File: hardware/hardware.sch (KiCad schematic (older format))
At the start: 23 parts, among them J1 6P6C, J2 RJ45_LED_Shielded, Q1 BUK7M33-60EX, U1 Teensy4.1_DEV-16771, U2 LT1910, U3 OKI, U4 OKI-78SR-3.3_1.5-W36H-C

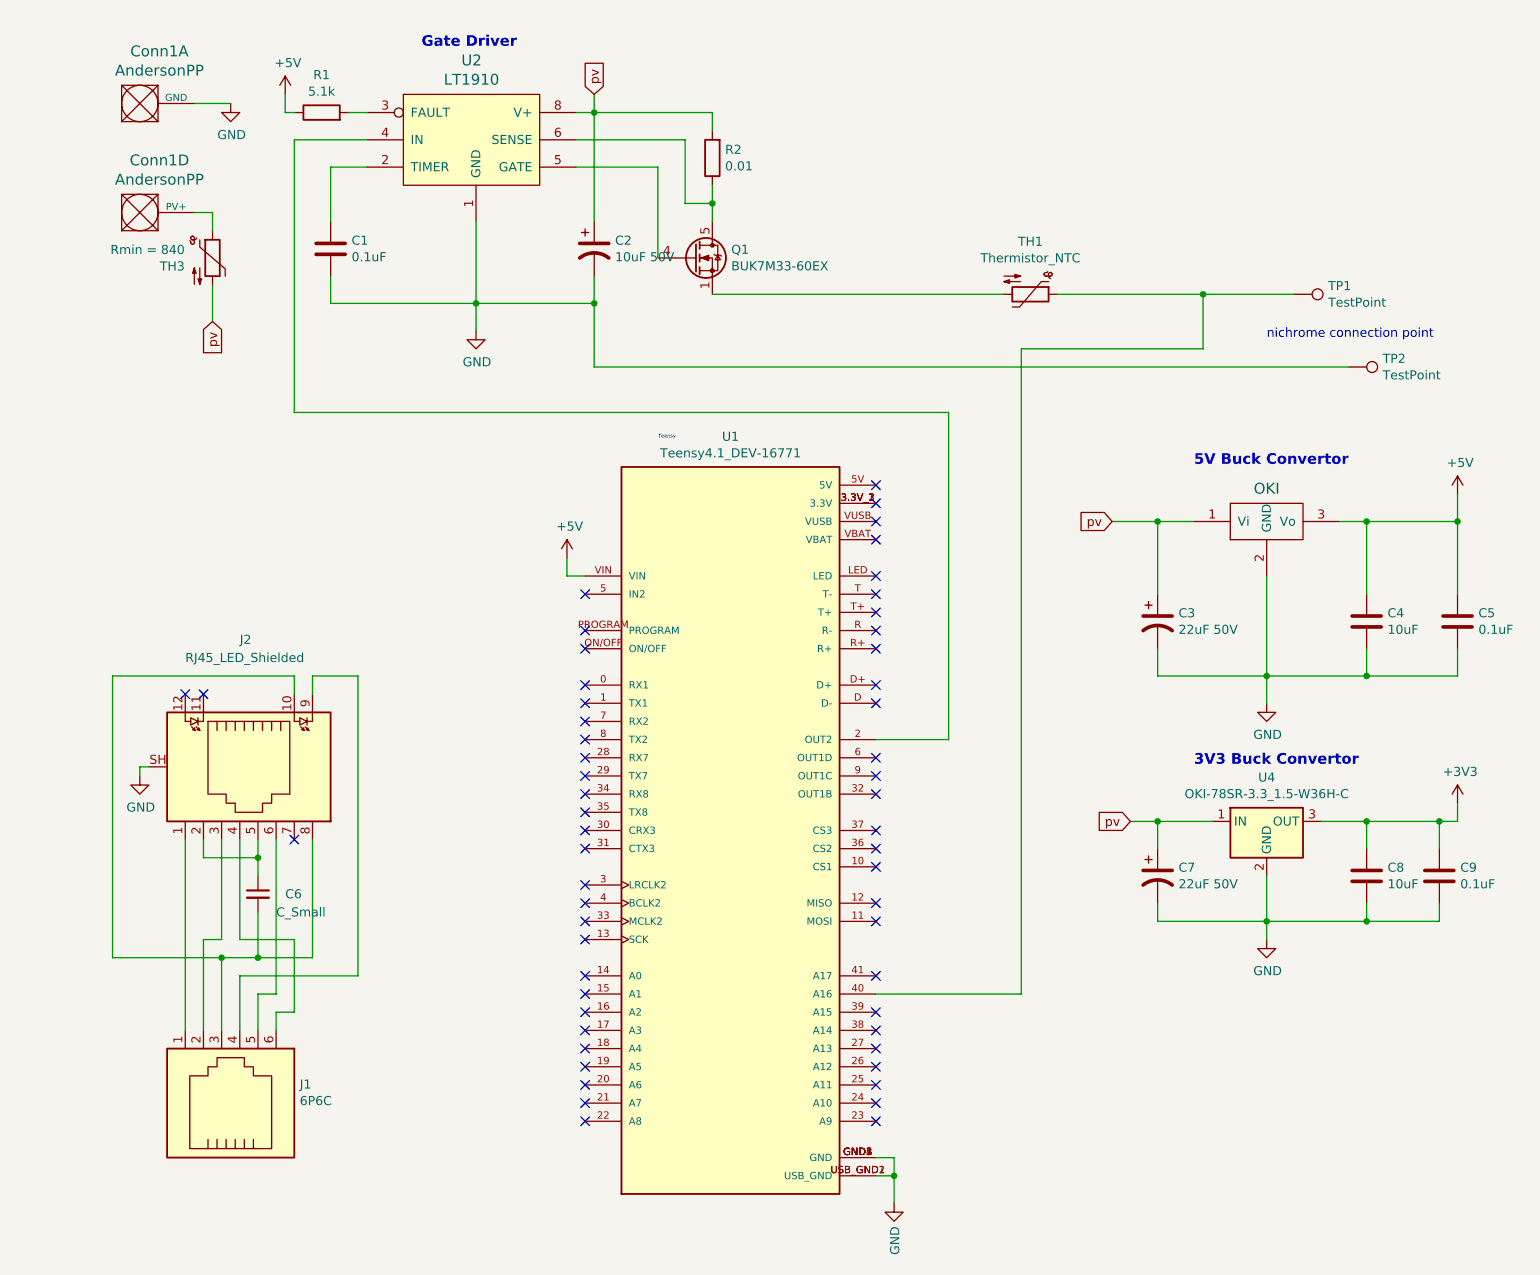
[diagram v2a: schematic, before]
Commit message: Fixed ethernet circuit and general cleaning
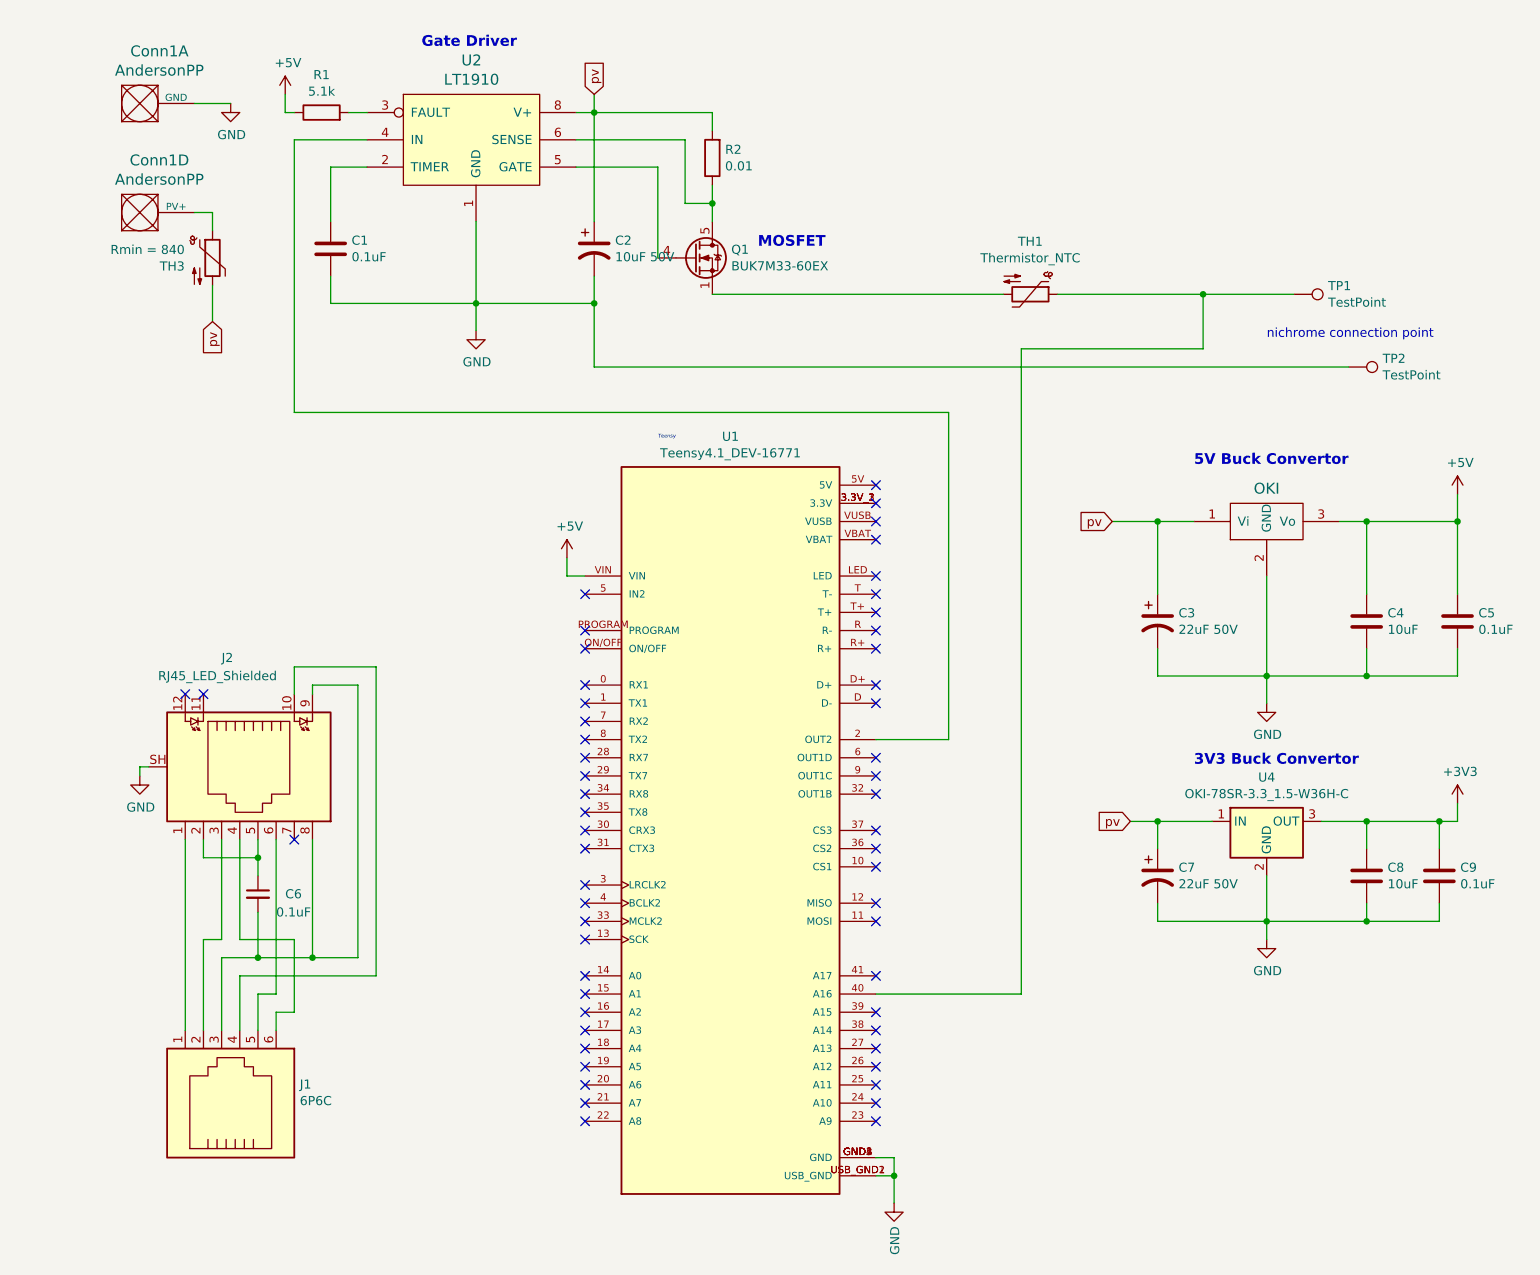
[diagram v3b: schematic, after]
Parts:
- C6: value C_Small -> 0.1uF
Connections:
- net at C6.2, J1.3, J2.8: now also J2.9; no longer J2.10
- net at J1.4: now also J2.10; no longer J2.9
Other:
- note added: "MOSFET"
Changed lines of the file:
@@
 U 1 1 61651929
 P 1350 4550
-F 0 "J2" V 650 4550 50  0000 L CNN
-F 1 "RJ45_LED_Shielded" V 750 4250 50  0000 L CNN
+F 0 "J2" V 750 4450 50  0000 L CNN
+F 1 "RJ45_LED_Shielded" V 850 4100 50  0000 L CNN
 F 2 "" V 1350 4575 50  0001 C CNN
 F 3 "~" V 1350 4575 50  0001 C CNN
@@
 $EndComp
 Wire Wire Line
-	2000 4050 1750 4050
+	2000 4100 1750 4100
 NoConn ~ 1650 4950
 NoConn ~ 1050 4150
@@
 P 1450 5250
 F 0 "C6" H 1600 5250 50  0000 L CNN
-F 1 "C_Small" H 1550 5150 50  0000 L CNN
+F 1 "0.1uF" H 1550 5150 50  0000 L CNN
 F 2 "" H 1450 5250 50  0001 C CNN
 F 3 "~" H 1450 5250 50  0001 C CNN
@@
 Wire Wire Line
 	1250 5500 1150 5500
-Wire Wire Line
-	1350 5700 2000 5700
 Wire Wire Line
 	1450 5800 1550 5800
@@
 	1350 5500 1350 4950
 Wire Wire Line
-	1250 5600 650  5600
+	1750 4100 1750 4150
 Wire Wire Line
-	650  5600 650  4050
+	1750 5600 2000 5600
 Wire Wire Line
-	650  4050 1650 4050
+	2000 5600 2000 4100
+Connection ~ 1750 5600
 Wire Wire Line
-	1650 4050 1650 4150
-Connection ~ 1250 5600
+	2100 5700 2100 4000
 Wire Wire Line
-	2000 4050 2000 5700
+	2100 4000 1650 4000
 Wire Wire Line
-	1750 4050 1750 4150
+	1350 5700 2100 5700
+Wire Wire Line
+	1650 4000 1650 4150
+Text Notes 4200 1700 0    59   ~ 12
+MOSFET
 $EndSCHEMATC

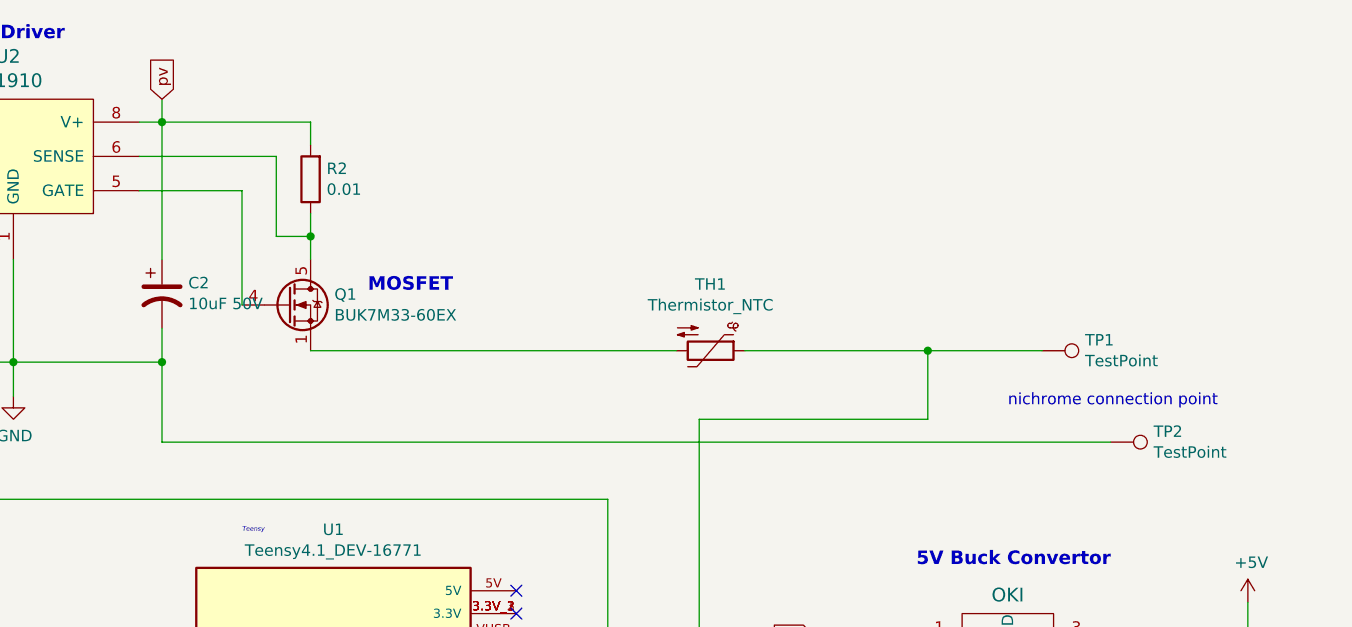
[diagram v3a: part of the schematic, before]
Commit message: Nichrome Cleanup
Cleaned up circuit for PDR and assigned R for wire
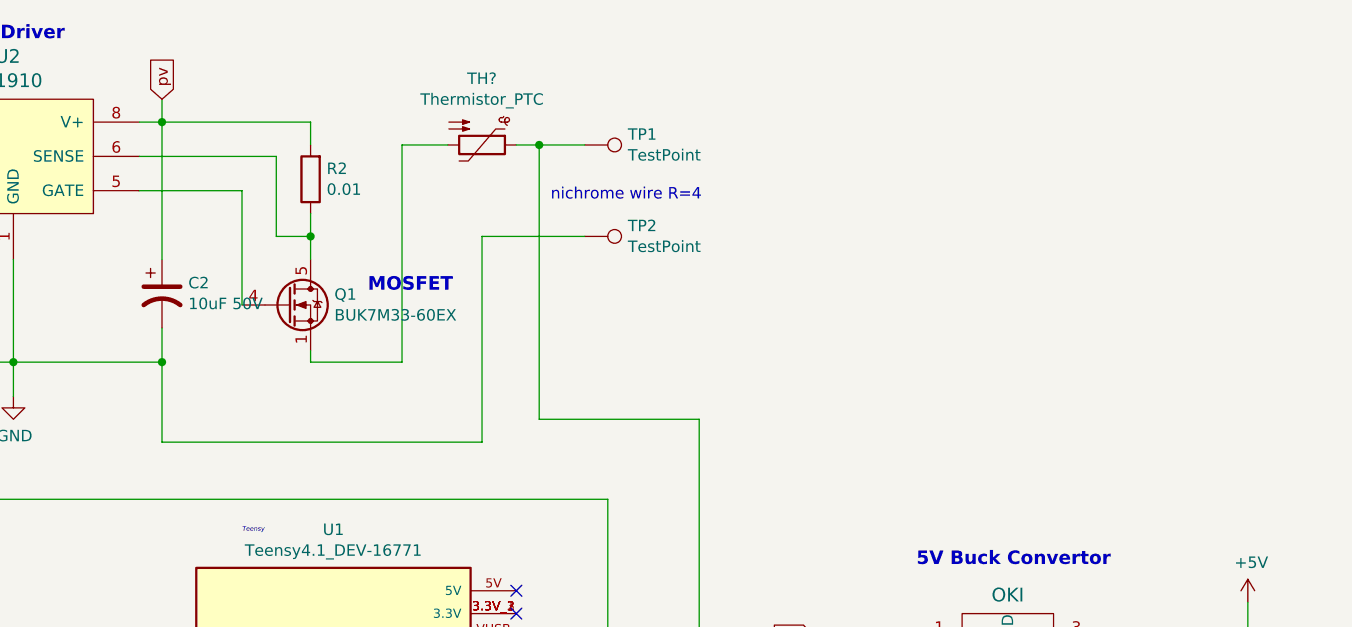
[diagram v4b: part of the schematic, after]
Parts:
- removed TH1: Thermistor_NTC, symbol Device:Thermistor_NTC
- added TH?: Thermistor_PTC, symbol Device:Thermistor_PTC
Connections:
- net at TP1.1, U1.40 (A16): now also TH?.1
- net at Q1.1 (S), Q1.2 (S), Q1.3 (S): now also TH?.2
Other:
- note added: "nichrome wire R=4"
- note removed: "nichrome connection point"
- moved on the sheet: TP1, TP2
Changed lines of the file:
@@
 Wire Wire Line
 	3150 3500 3250 3500
-$Comp
-L Device:Thermistor_NTC TH1
-U 1 1 615942DB
-P 5700 1950
-F 0 "TH1" V 5410 1950 50  0000 C CNN
-F 1 "Thermistor_NTC" V 5501 1950 50  0000 C CNN
-F 2 "" H 5700 2000 50  0001 C CNN
-F 3 "~" H 5700 2000 50  0001 C CNN
-	1    5700 1950
-	0    1    1    0
-$EndComp
 Wire Wire Line
 	5250 2600 1650 2600
@@
 Wire Wire Line
 	5650 5800 5650 2250
-Wire Wire Line
-	5650 2250 6650 2250
 $Comp
 L Device:Thermistor_NTC TH3
@@
 Wire Wire Line
 	1200 1500 1200 1600
-$Comp
-L Connector:TestPoint TP1
-U 1 1 6164E01B
-P 7150 1950
-F 0 "TP1" V 7104 2138 50  0000 L CNN
-F 1 "TestPoint" V 7195 2138 50  0000 L CNN
-F 2 "" H 7350 1950 50  0001 C CNN
-F 3 "~" H 7350 1950 50  0001 C CNN
-	1    7150 1950
-	0    1    1    0
-$EndComp
-$Comp
-L Connector:TestPoint TP2
-U 1 1 616506C1
-P 7450 2350
-F 0 "TP2" V 7404 2538 50  0000 L CNN
-F 1 "TestPoint" V 7495 2538 50  0000 L CNN
-F 2 "" H 7650 2350 50  0001 C CNN
-F 3 "~" H 7650 2350 50  0001 C CNN
-	1    7450 2350
-	0    1    1    0
-$EndComp
 $Comp
 L Connector:RJ45_LED_Shielded J2
@@
 	3300 2350 3300 2000
 Connection ~ 3300 2000
-Wire Wire Line
-	3300 2350 7450 2350
-Wire Wire Line
-	6650 2250 6650 1950
-Connection ~ 6650 1950
-Wire Wire Line
-	6650 1950 7150 1950
-Wire Wire Line
-	3950 1950 5550 1950
 NoConn ~ 4850 5700
 $Comp
@@
 	4950 6950 4950 6800
 Connection ~ 4950 6800
-Wire Wire Line
-	5850 1950 6650 1950
-Text Notes 7000 2200 0    50   ~ 0
-nichrome connection point
 Wire Wire Line
 	800  4600 800  4550
@@
 Text Notes 4200 1700 0    59   ~ 12
 MOSFET
+$Comp
+L Device:Thermistor_PTC TH?
+U 1 1 616AD776
+P 4700 1050
+F 0 "TH?" V 4410 1050 50  0000 C CNN
+F 1 "Thermistor_PTC" V 4501 1050 50  0000 C CNN
+F 2 "" H 4750 850 50  0001 L CNN
+F 3 "~" H 4700 1050 50  0001 C CNN
+	1    4700 1050
+	0    1    1    0
+$EndComp
+Wire Wire Line
+	3950 1950 3950 2000
+Wire Wire Line
+	3950 2000 4350 2000
+Wire Wire Line
+	4350 2000 4350 1050
+Wire Wire Line
+	4350 1050 4550 1050
+$Comp
+L Connector:TestPoint TP1
+U 1 1 6164E01B
+P 5150 1050
+F 0 "TP1" V 5104 1238 50  0000 L CNN
+F 1 "TestPoint" V 5195 1238 50  0000 L CNN
+F 2 "" H 5350 1050 50  0001 C CNN
+F 3 "~" H 5350 1050 50  0001 C CNN
+	1    5150 1050
+	0    1    1    0
+$EndComp
+$Comp
+L Connector:TestPoint TP2
+U 1 1 616506C1
+P 5150 1450
+F 0 "TP2" V 5104 1638 50  0000 L CNN
+F 1 "TestPoint" V 5195 1638 50  0000 L CNN
+F 2 "" H 5350 1450 50  0001 C CNN
+F 3 "~" H 5350 1450 50  0001 C CNN
+	1    5150 1450
+	0    1    1    0
+$EndComp
+Text Notes 5000 1300 0    50   ~ 0
+nichrome wire R=4
+Wire Wire Line
+	5650 2250 4950 2250
+Wire Wire Line
+	4950 2250 4950 1050
+Wire Wire Line
+	4950 1050 4850 1050
+Wire Wire Line
+	5150 1050 4950 1050
+Connection ~ 4950 1050
+Wire Wire Line
+	5150 1450 4700 1450
+Wire Wire Line
+	4700 1450 4700 2350
+Wire Wire Line
+	4700 2350 3300 2350
 $EndSCHEMATC
